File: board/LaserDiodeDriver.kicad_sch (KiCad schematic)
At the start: 55 parts, among them J1 Conn_01x02, K4 EE2-12NU, Q1 2N7002, Q2 IRF9Z34, SW1 SW_SPDT, U1 LM317_TO-220, U2 OPA4192, U3 LT1009

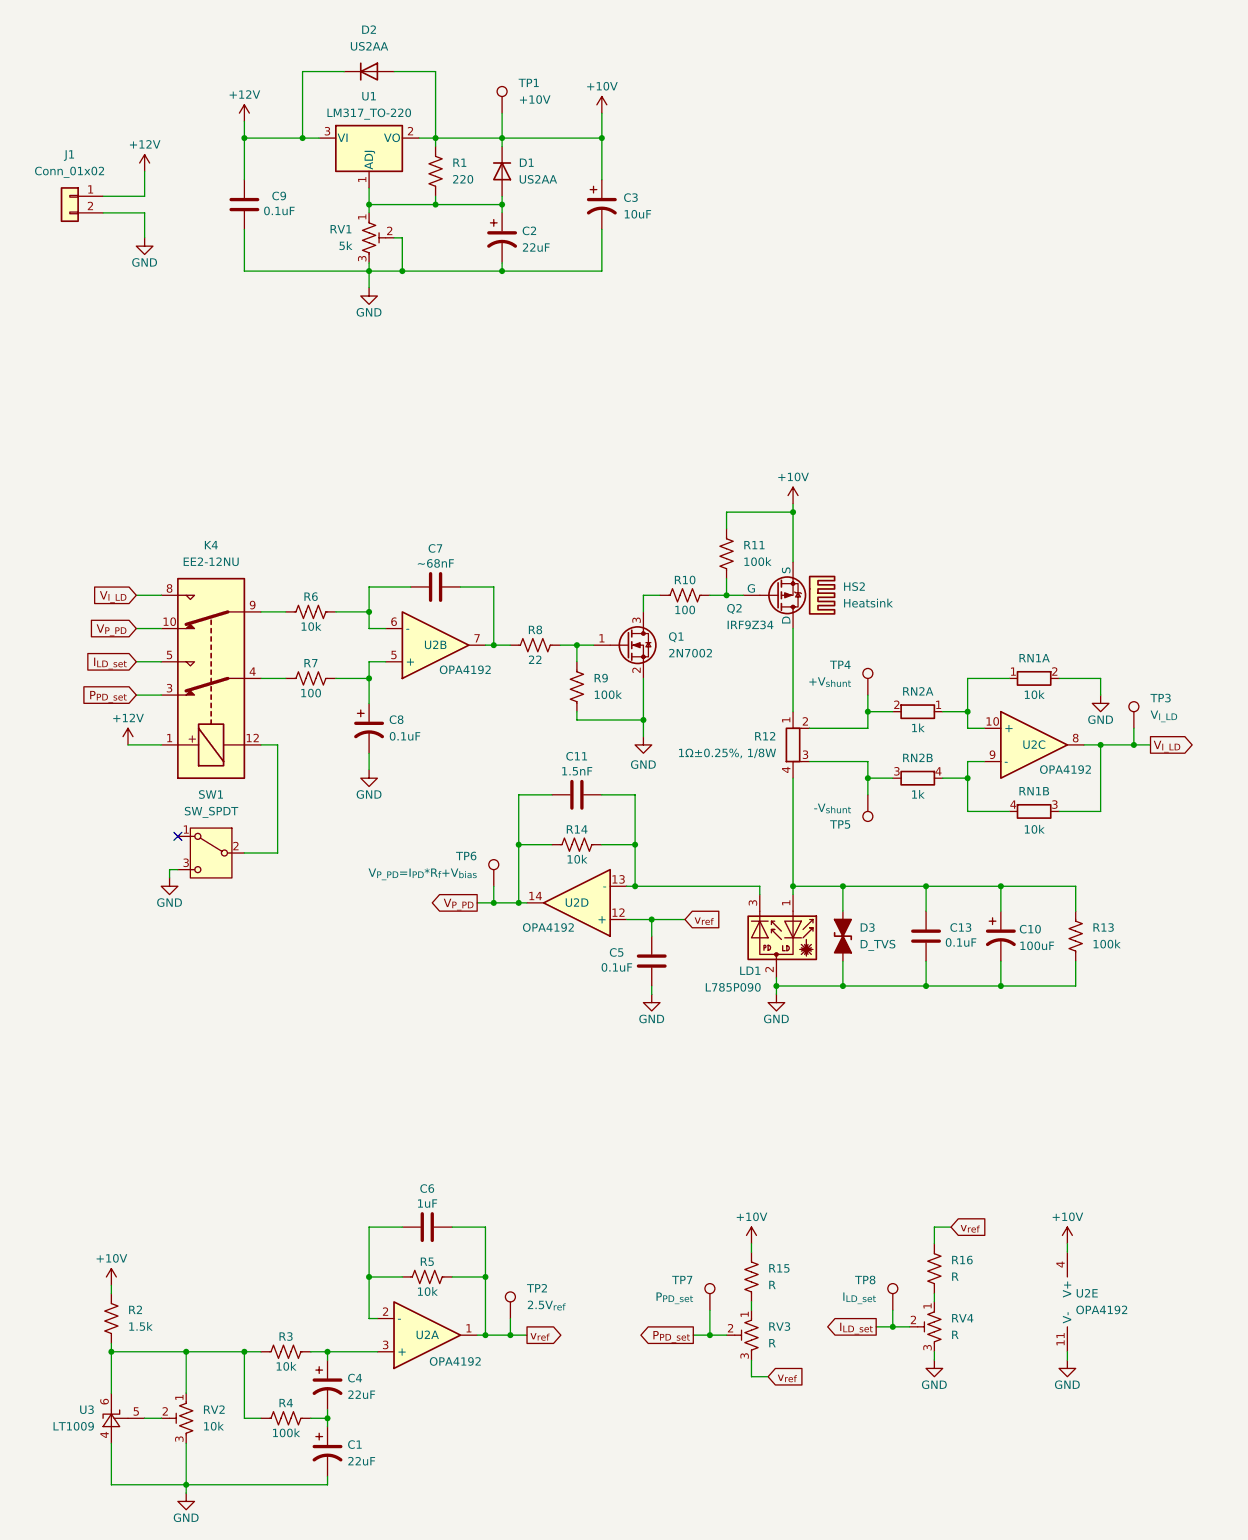
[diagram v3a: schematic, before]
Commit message: Got a footprint, description, price, and datasheet for all parts except laser diode socket
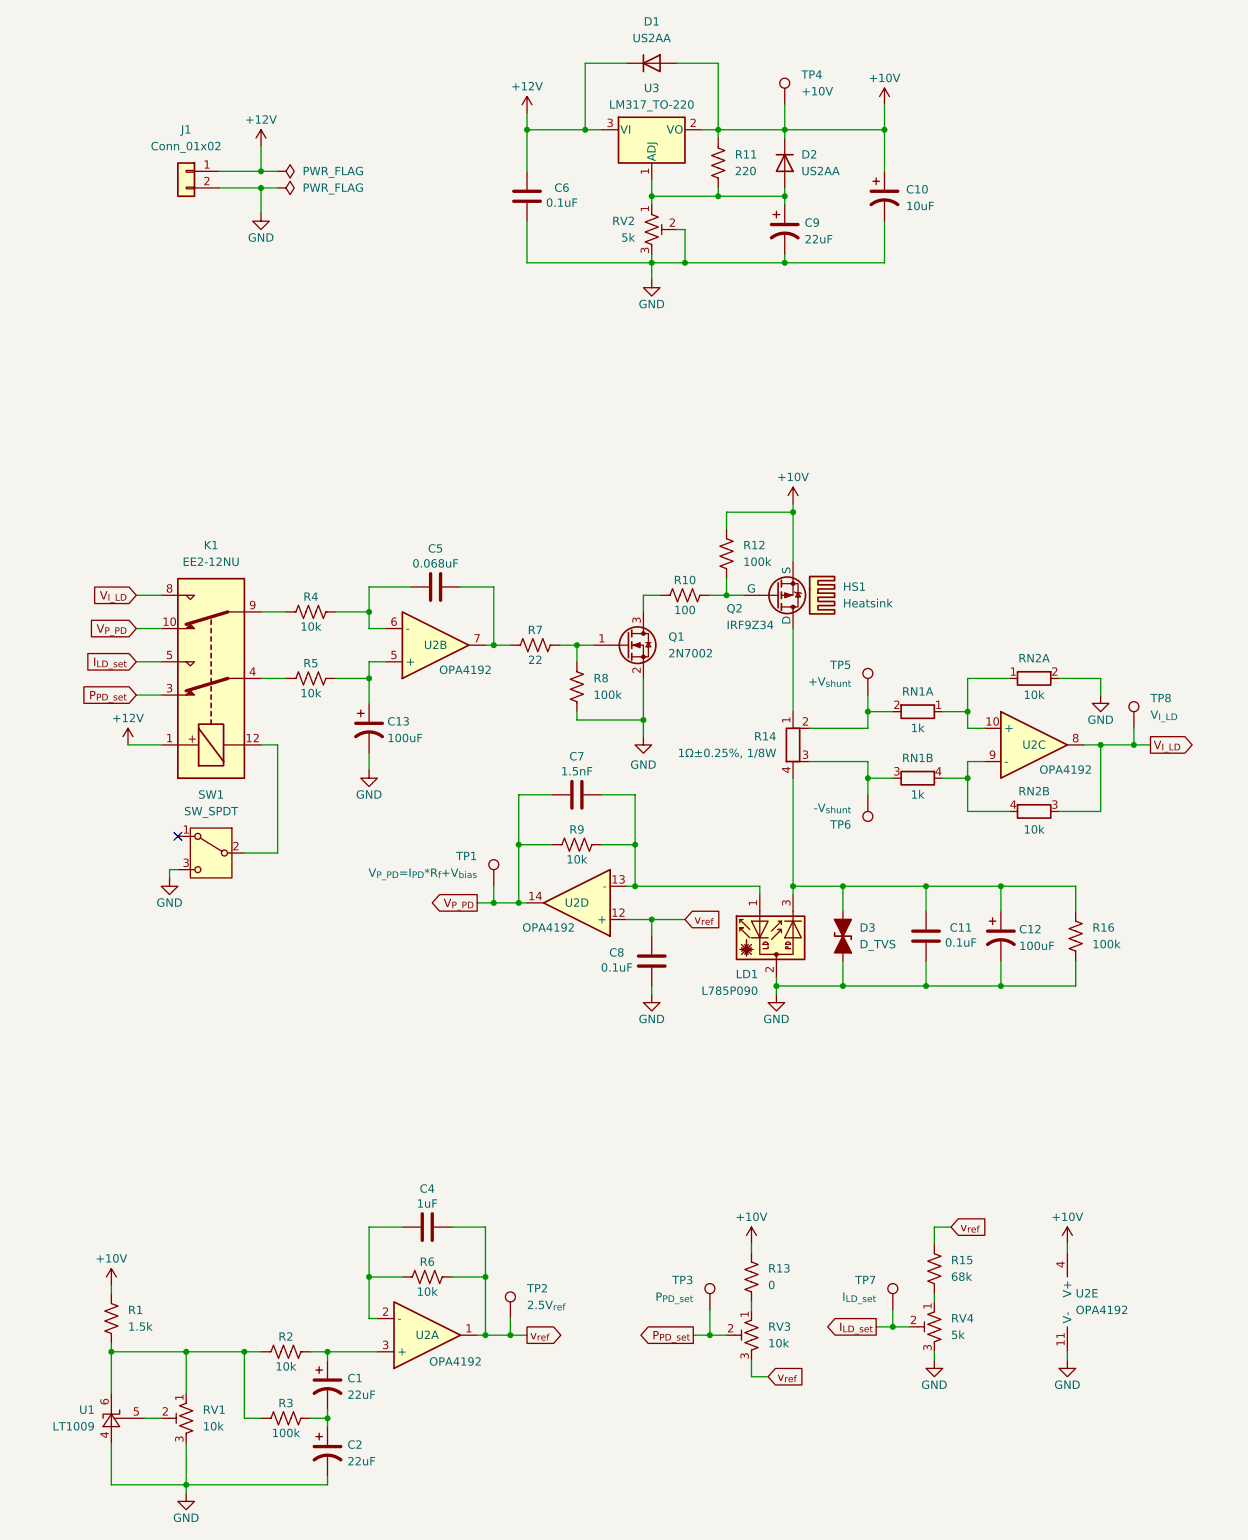
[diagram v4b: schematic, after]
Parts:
- removed C8: 0.1uF, symbol Device:C_Polarized_US
- removed R7: 100, Resistor_SMD:R_0603_1608Metric, symbol Device:R_US
- added C13: 100uF, Capacitor_SMD:CP_Elec_6.3x5.8, symbol Device:C_Polarized_US
- added R5: 10k, Resistor_SMD:R_0603_1608Metric, symbol Device:R_US
- C5: renamed from C7; value ~68nF -> 0.068uF; footprint (none) -> Capacitor_SMD:C_0603_1608Metric; Price (none) -> $0.10000
- LD1: footprint (none) -> Connector_RJ:RJ45_Pulse_JK0654219NL_Horizontal
- R11: renamed from R1; footprint (none) -> Resistor_SMD:R_0603_1608Metric
- R13: renamed from R15; value R -> 0; footprint (none) -> Resistor_SMD:R_0603_1608Metric
- R15: renamed from R16; value R -> 68k; footprint (none) -> Capacitor_SMD:C_0603_1608Metric; Price (none) -> $0.10000
- RV3: value R -> 10k; footprint (none) -> Potentiometer_THT:Potentiometer_Bourns_3296W_Vertical; Price (none) -> $2.05000
- RV4: value R -> 5k; footprint (none) -> Potentiometer_THT:Potentiometer_Bourns_3296Y_Vertical; Price (none) -> $2.05000
- renumbered C4 to C1, C3 to C10, C13 to C11, C10 to C12, C1 to C2, C6 to C4, C9 to C6, C11 to C7, C5 to C8, C2 to C9, D2 to D1, D1 to D2, HS2 to HS1, K4 to K1, R2 to R1, R11 to R12, R12 to R14, R13 to R16, R3 to R2, R4 to R3, R6 to R4, R5 to R6, R8 to R7, R9 to R8, R14 to R9, RN2 to RN1, RN1 to RN2, RV2 to RV1, RV1 to RV2, TP6 to TP1, TP7 to TP3, TP1 to TP4, TP4 to TP5, TP5 to TP6, TP8 to TP7, TP3 to TP8, U3 to U1, U1 to U3
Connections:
- net GND: now also C13.2
- net at K1.4: now also R5.1
- net at U2.5 (+): now also C13.1, R5.2
- net at C11.1, C12.1, D3.2 (A2)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: now also LD1.3; no longer LD1.1
- net at C7.2, R9.2, U2.13 (-): now also LD1.1; no longer LD1.3
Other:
- moved on the sheet: C10, C6, C9, D1, D2, J1, R11, RV2, TP4, U3

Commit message: Made custom footprint/3D model for laser diode socket
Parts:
- LD1: footprint Connector_RJ:RJ45_Pulse_JK0654219NL_Horizontal -> LD_Library:S7060R - Laser Diode Socket for Ø5.6 mm Laser, 3 Pin
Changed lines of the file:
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@@
 	)
 	(symbol
-		(lib_name "D_Laser_Photo_PType_1")
 		(lib_id "Device:D_Laser_Photo_PType")
 		(at 132.08 161.29 90)
@@
 			)
 		)
-		(property "Footprint" "Connector_RJ:RJ45_Pulse_JK0654219NL_Horizontal"
+		(property "Footprint" "LD_Library:S7060R - Laser Diode Socket for Ø5.6 mm Laser, 3 Pin"
 			(at 130.175 161.29 0)
 			(effects
@@
 			)
 		)
-		(property "Datasheet" "https://www.thorlabs.com/thorproduct.cfm?partnumber=L785P090"
+		(property "Datasheet" "http://www.egismos.disonhu.com/laser/diode-package.htm"
 			(at 134.62 157.988 0)
 			(effects
@@
 			)
 		)
-		(property "Description" "785 nm Fabry-Perot Laser Diode, 90 mW"
+		(property "Description" "Laser diode with photodiode, center on pin 2, PD cathode on pin 3"
 			(at 132.08 161.29 0)
 			(effects

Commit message: Shunt Sense footprint
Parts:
- R14: footprint Resistor_SMD:R_0805_2012Metric -> LD_Library:R_Shunt_0805_2012Metric
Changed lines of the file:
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@@
 			)
 		)
-		(property "Footprint" "Resistor_SMD:R_0805_2012Metric"
+		(property "Footprint" "LD_Library:R_Shunt_0805_2012Metric"
 			(at 132.842 130.81 90)
 			(effects

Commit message: Trying goofy layout things
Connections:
- net GND: now also RN2.3 (R2.1); no longer RN2.2 (R1.2)
- net V_{I_LD}: now also RN2.1 (R1.1), U2.7; no longer RN2.3 (R2.1), U2.8
- net V_{P_PD}: now also U2.1; no longer U2.14
- net v_{ref}: now also U2.14, U2.3 (+); no longer U2.1, U2.12 (+)
- net at C5.1, R4.2: now also U2.9 (-); no longer U2.6 (-)
- net at C5.2, R7.1: now also U2.8; no longer U2.7
- net at C7.2, LD1.1, R9.2: now also U2.2 (-); no longer U2.13 (-)
- net at C4.1, R6.1: now also U2.13 (-); no longer U2.2 (-)
- net at C1.1, R2.2: now also U2.12 (+); no longer U2.3 (+)
- net at C13.1, R5.2: now also U2.10 (+); no longer U2.5 (+)
- new net: RN1.1 (R1.1), RN2.4 (R2.2), U2.5 (+)
- new net: RN1.4 (R2.2), RN2.2 (R1.2), U2.6 (-)
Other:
- moved on the sheet: RN2A, RN2B, U2A, U2B, U2C, U2D
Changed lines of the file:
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@@
 	(symbol
 		(lib_id "Device:Opamp_Quad")
-		(at 171.45 130.81 0)
+		(at 80.01 115.57 0)
+		(mirror x)
 		(unit 3)
 		(exclude_from_sim no)
@@
 		(dnp no)
 		(property "Reference" "U2"
-			(at 171.45 130.81 0)
+			(at 80.01 115.57 0)
 			(effects
 				(font
@@
 		)
 		(property "Value" "OPA4192"
-			(at 176.276 134.62 0)
+			(at 84.836 111.76 0)
 			(effects
 				(font
@@
 		)
 		(property "Footprint" "Package_SO:SOIC-14_3.9x8.7mm_P1.27mm"
-			(at 171.45 130.81 0)
+			(at 80.01 115.57 0)
 			(effects
 				(font
@@
 		)
 		(property "Datasheet" "https://www.digikey.com/en/products/detail/texas-instruments/OPA4192IDR/5647258"
-			(at 171.45 130.81 0)
+			(at 80.01 115.57 0)
 			(effects
 				(font
@@
 		)
 		(property "Description" "Standard (General Purpose) Amplifier 4 Circuit Rail-to-Rail 14-SOIC"
-			(at 171.45 130.81 0)
+			(at 80.01 115.57 0)
 			(effects
 				(font
@@
 		)
 		(property "Price" " $7.18000"
-			(at 171.45 130.81 0)
+			(at 80.01 115.57 0)
 			(effects
 				(font
@@
 		)
 		(property "Sim.Library" "${KICAD9_SYMBOL_DIR}/Simulation_SPICE.sp"
-			(at 171.45 130.81 0)
+			(at 80.01 115.57 0)
 			(effects
 				(font
@@
 		)
 		(property "Sim.Name" "kicad_builtin_opamp_quad"
-			(at 171.45 130.81 0)
+			(at 80.01 115.57 0)
 			(effects
 				(font
@@
 		)
 		(property "Sim.Device" "SUBCKT"
-			(at 171.45 130.81 0)
+			(at 80.01 115.57 0)
 			(effects
 				(font
@@
 		)
 		(property "Sim.Pins" "1=out1 2=in1- 3=in1+ 4=vcc 5=in2+ 6=in2- 7=out2 8=out3 9=in3- 10=in3+ 11=vee 12=in4+ 13=in4- 14=out4"
-			(at 171.45 130.81 0)
+			(at 80.01 115.57 0)
 			(effects
 				(font
@@
 	(symbol
 		(lib_id "Device:R_Pack02_SIP_Split")
-		(at 171.45 140.97 90)
+		(at 171.45 120.65 90)
 		(unit 2)
 		(exclude_from_sim no)
@@
 		(dnp no)
 		(property "Reference" "RN2"
-			(at 171.45 137.922 90)
+			(at 171.45 117.602 90)
 			(effects
 				(font
@@
 		)
 		(property "Value" "10k"
-			(at 171.45 143.764 90)
+			(at 171.45 123.444 90)
 			(effects
 				(font
@@
 		)
 		(property "Footprint" "Resistor_SMD:R_Array_Convex_2x0606"
-			(at 171.45 143.002 90)
+			(at 171.45 122.682 90)
 			(effects
 				(font
@@
 		)
 		(property "Datasheet" "https://www.digikey.com/en/products/detail/vishay/ACASN1002S1002P1AT/4725785"
-			(at 171.45 140.97 0)
+			(at 171.45 120.65 0)
 			(effects
 				(font
@@
 		)
 		(property "Description" "10k Ohm ±0.1% 125mW Power Per Element Isolated 2 Resistor Network/Array ±25ppm/°C 0606, Convex"
-			(at 171.45 140.97 0)
+			(at 171.45 120.65 0)
 			(effects
 				(font
@@
 		)
 		(property "Price" " $0.72000"
-			(at 171.45 140.97 90)
+			(at 171.45 120.65 90)
 			(effects
 				(font
@@
 	(symbol
 		(lib_id "Device:Opamp_Quad")
-		(at 101.6 154.94 180)
+		(at 78.74 220.98 0)
+		(mirror x)
 		(unit 4)
 		(exclude_from_sim no)
@@
 		(dnp no)
 		(property "Reference" "U2"
-			(at 101.6 154.94 0)
+			(at 78.74 220.98 0)
 			(effects
 				(font
@@
 		)
 		(property "Value" "OPA4192"
-			(at 97.282 158.75 0)
+			(at 83.058 224.79 0)
 			(effects
 				(font
@@
 		)
 		(property "Footprint" "Package_SO:SOIC-14_3.9x8.7mm_P1.27mm"
-			(at 101.6 154.94 0)
+			(at 78.74 220.98 0)
 			(effects
 				(font
@@
 		)
 		(property "Datasheet" "https://www.digikey.com/en/products/detail/texas-instruments/OPA4192IDR/5647258"
-			(at 101.6 154.94 0)
+			(at 78.74 220.98 0)
 			(effects
 				(font
@@
 		)
 		(property "Description" "Standard (General Purpose) Amplifier 4 Circuit Rail-to-Rail 14-SOIC"
-			(at 101.6 154.94 0)
+			(at 78.74 220.98 0)
 			(effects
 				(font
@@
 		)
 		(property "Price" " $7.18000"
-			(at 101.6 154.94 0)
+			(at 78.74 220.98 0)
 			(effects
 				(font
@@
 		)
 		(property "Sim.Library" "${KICAD9_SYMBOL_DIR}/Simulation_SPICE.sp"
-			(at 101.6 154.94 0)
+			(at 78.74 220.98 0)
 			(effects
 				(font
@@
 		)
 		(property "Sim.Name" "kicad_builtin_opamp_quad"
-			(at 101.6 154.94 0)
+			(at 78.74 220.98 0)
 			(effects
 				(font
@@
 		)
 		(property "Sim.Device" "SUBCKT"
-			(at 101.6 154.94 0)
+			(at 78.74 220.98 0)
 			(effects
 				(font
@@
 		)
 		(property "Sim.Pins" "1=out1 2=in1- 3=in1+ 4=vcc 5=in2+ 6=in2- 7=out2 8=out3 9=in3- 10=in3+ 11=vee 12=in4+ 13=in4- 14=out4"
-			(at 101.6 154.94 0)
+			(at 78.74 220.98 0)
 			(effects
 				(font
@@
 	(symbol
 		(lib_id "Device:Opamp_Quad")
-		(at 80.01 115.57 0)
-		(mirror x)
+		(at 171.45 130.81 0)
 		(unit 2)
 		(exclude_from_sim no)
@@
 		(dnp no)
 		(property "Reference" "U2"
-			(at 80.01 115.57 0)
+			(at 171.45 130.81 0)
 			(effects
 				(font
@@
 		)
 		(property "Value" "OPA4192"
-			(at 84.582 119.38 0)
+			(at 176.276 134.366 0)
 			(effects
 				(font
@@
 		)
 		(property "Footprint" "Package_SO:SOIC-14_3.9x8.7mm_P1.27mm"
-			(at 80.01 115.57 0)
+			(at 171.45 130.81 0)
 			(effects
 				(font
@@
 		)
 		(property "Datasheet" "https://www.digikey.com/en/products/detail/texas-instruments/OPA4192IDR/5647258"
-			(at 80.01 115.57 0)
+			(at 171.45 130.81 0)
 			(effects
 				(font
@@
 		)
 		(property "Description" "Standard (General Purpose) Amplifier 4 Circuit Rail-to-Rail 14-SOIC"
-			(at 80.01 115.57 0)
+			(at 171.45 130.81 0)
 			(effects
 				(font
@@
 		)
 		(property "Price" " $7.18000"
-			(at 80.01 115.57 0)
+			(at 171.45 130.81 0)
 			(effects
 				(font
@@
 		)
 		(property "Sim.Library" "${KICAD9_SYMBOL_DIR}/Simulation_SPICE.sp"
-			(at 80.01 115.57 0)
+			(at 171.45 130.81 0)
 			(effects
 				(font
@@
 		)
 		(property "Sim.Name" "kicad_builtin_opamp_quad"
-			(at 80.01 115.57 0)
+			(at 171.45 130.81 0)
 			(effects
 				(font
@@
 		)
 		(property "Sim.Device" "SUBCKT"
-			(at 80.01 115.57 0)
+			(at 171.45 130.81 0)
 			(effects
 				(font
@@
 		)
 		(property "Sim.Pins" "1=out1 2=in1- 3=in1+ 4=vcc 5=in2+ 6=in2- 7=out2 8=out3 9=in3- 10=in3+ 11=vee 12=in4+ 13=in4- 14=out4"
-			(at 80.01 115.57 0)
+			(at 171.45 130.81 0)
 			(effects
 				(font
@@
 	(symbol
 		(lib_id "Device:R_Pack02_SIP_Split")
-		(at 171.45 120.65 270)
-		(mirror x)
+		(at 171.45 140.97 90)
 		(unit 1)
 		(exclude_from_sim no)
@@
 		(dnp no)
 		(property "Reference" "RN2"
-			(at 171.45 117.602 90)
+			(at 171.45 137.922 90)
 			(effects
 				(font
@@
 		)
 		(property "Value" "10k"
-			(at 171.45 123.19 90)
+			(at 171.45 143.51 90)
 			(effects
 				(font
@@
 		)
 		(property "Footprint" "Resistor_SMD:R_Array_Convex_2x0606"
-			(at 171.45 122.682 90)
+			(at 171.45 143.002 90)
 			(effects
 				(font
@@
 		)
 		(property "Datasheet" "https://www.digikey.com/en/products/detail/vishay/ACASN1002S1002P1AT/4725785"
-			(at 171.45 120.65 0)
+			(at 171.45 140.97 0)
 			(effects
 				(font
@@
 		)
 		(property "Description" "10k Ohm ±0.1% 125mW Power Per Element Isolated 2 Resistor Network/Array ±25ppm/°C 0606, Convex"
-			(at 171.45 120.65 0)
+			(at 171.45 140.97 0)
 			(effects
 				(font
@@
 		)
 		(property "Price" " $0.72000"
-			(at 171.45 120.65 90)
+			(at 171.45 140.97 90)
 			(effects
 				(font
@@
 	(symbol
 		(lib_id "Device:Opamp_Quad")
-		(at 78.74 220.98 0)
-		(mirror x)
+		(at 101.6 154.94 180)
 		(unit 1)
 		(exclude_from_sim no)
@@
 		(dnp no)
 		(property "Reference" "U2"
-			(at 78.74 220.98 0)
+			(at 101.6 154.94 0)
 			(effects
 				(font
@@
 		)
 		(property "Value" "OPA4192"
-			(at 83.058 225.044 0)
+			(at 97.282 159.004 0)
 			(effects
 				(font
@@
 		)
 		(property "Footprint" "Package_SO:SOIC-14_3.9x8.7mm_P1.27mm"
-			(at 78.74 220.98 0)
+			(at 101.6 154.94 0)
 			(effects
 				(font
@@
 		)
 		(property "Datasheet" "https://www.digikey.com/en/products/detail/texas-instruments/OPA4192IDR/5647258"
-			(at 78.74 220.98 0)
+			(at 101.6 154.94 0)
 			(effects
 				(font
@@
 		)
 		(property "Description" "Standard (General Purpose) Amplifier 4 Circuit Rail-to-Rail 14-SOIC"
-			(at 78.74 220.98 0)
+			(at 101.6 154.94 0)
 			(effects
 				(font
@@
 		)
 		(property "Price" " $7.18000"
-			(at 78.74 220.98 0)
+			(at 101.6 154.94 0)
 			(effects
 				(font
@@
 		)
 		(property "Sim.Library" "${KICAD9_SYMBOL_DIR}/Simulation_SPICE.sp"
-			(at 78.74 220.98 0)
+			(at 101.6 154.94 0)
 			(effects
 				(font
@@
 		)
 		(property "Sim.Name" "kicad_builtin_opamp_quad"
-			(at 78.74 220.98 0)
+			(at 101.6 154.94 0)
 			(effects
 				(font
@@
 		)
 		(property "Sim.Device" "SUBCKT"
-			(at 78.74 220.98 0)
+			(at 101.6 154.94 0)
 			(effects
 				(font
@@
 		)
 		(property "Sim.Pins" "1=out1 2=in1- 3=in1+ 4=vcc 5=in2+ 6=in2- 7=out2 8=out3 9=in3- 10=in3+ 11=vee 12=in4+ 13=in4- 14=out4"
-			(at 78.74 220.98 0)
+			(at 101.6 154.94 0)
 			(effects
 				(font

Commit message: Final pricing of components $44.88
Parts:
- D1, D2: Price (none) -> $0.40000
- K1: Price (none) -> $2.27000
- LD1: LD_Datasheet (none) -> http://www.egismos.disonhu.com/laser/diode-package.htm; Price $54.02 -> $7.49
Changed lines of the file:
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@@
 			)
 		)
-		(property "Datasheet" "http://www.egismos.disonhu.com/laser/diode-package.htm"
+		(property "Datasheet" "https://www.thorlabs.com/thorproduct.cfm?partnumber=S7060R"
 			(at 134.62 157.988 0)
 			(effects
@@
 			)
 		)
-		(property "Price" "$54.02"
+		(property "Price" "$7.49"
+			(at 132.08 161.29 90)
+			(effects
+				(font
+					(size 1.27 1.27)
+				)
+				(hide yes)
+			)
+		)
+		(property "LD_Datasheet" "http://www.egismos.disonhu.com/laser/diode-package.htm"
 			(at 132.08 161.29 90)
 			(effects
@@
 			)
 		)
+		(property "Price" " $0.40000"
+			(at 113.03 26.67 0)
+			(effects
+				(font
+					(size 1.27 1.27)
+				)
+				(hide yes)
+			)
+		)
 		(pin "1"
 		)
@@
 			)
 		)
+		(property "Price" " $0.40000"
+			(at 133.35 41.91 90)
+			(effects
+				(font
+					(size 1.27 1.27)
+				)
+				(hide yes)
+			)
+		)
 		(pin "1"
 		)
@@
 			)
 		)
-		(property "Datasheet" "https://content.kemet.com/datasheets/KEM_R7002_EC2_EE2.pdf"
+		(property "Datasheet" "https://www.digikey.com/en/products/detail/kemet/EE2-12NU/4291099"
 			(at 45.72 120.65 0)
 			(effects
@@
 			)
 		)
-		(property "Description" "General purpose signal relay, Kemet EE2 Series, DPDT (2 Form C), non-latching, SMD, 60W/125VA, 220VDC/250VAC, 2A, 12V DC coil"
+		(property "Description" "General Purpose Relay DPDT (2 Form C) Surface Mount"
 			(at 45.72 120.65 0)
 			(effects
 				(font
+					(size 1.27 1.27)
+				)
+				(hide yes)
+			)
+		)
+		(property "Price" " $2.27000"
+			(at 45.72 120.65 90)
+			(effects
+				(font
